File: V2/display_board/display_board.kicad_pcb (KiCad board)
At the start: 2 copper layers, 95 x 103.5 mm, 55 parts, among them J1 Conn_01x12, J2 Conn_01x12, Q1 Si1308EDL, SW1 SW_Push, SW2 SW_Push, SW3 SW_Push, SW4 SW_Push, U1 TPS61165DBV, U2 LTR-303ALS-01, U3 DS18B20Z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

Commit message: main board in good spot
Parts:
- moved J2 134.8 mm to (4.91, 103.1)
- moved J1 41.3 mm to (13.7, 102.8)
- moved C16 6.70 mm to (134.5, 57.5)
- moved U4 6.70 mm to (129.7, 57.1)
- moved H2 6.67 mm to (145.5, 54.5), turned to 180 degrees
- moved H4 6.67 mm to (145.5, 149.0)
- moved C1 3.00 mm to (84.8, 112.7)
- moved C10 3.00 mm to (85.8, 121.2)
- moved C11 3.00 mm to (86.0, 103.8)
- moved C12 3.00 mm to (93.5, 106.0)
- moved C13 3.00 mm to (95.8, 106.8)
- moved C15 3.00 mm to (100.2, 74.7)
- moved C2 3.00 mm to (77.5, 116.2)
- moved C3 3.00 mm to (81.0, 108.2)
- moved C4 3.00 mm to (80.2, 121.2)
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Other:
- board size 95 x 103.5 mm -> 100 x 103.5 mm

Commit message: Display board in good spot
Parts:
- removed J1, J2: Conn_01x12, Connector_PinHeader_2.54mm:PinHeader_1x12_P2.54mm_Vertical_SMD_Pin1Left
- added D7: GREEN, LED_SMD:LED_0805_2012Metric, F.Cu at (65.0, 56.5)
- added D8: RED, LED_SMD:LED_0805_2012Metric, F.Cu at (75.0, 56.5)
- added J5: Conn_02x14_Top_Bottom, Connector_PinHeader_2.54mm:PinHeader_2x14_P2.54mm_Vertical_SMD, B.Cu at (106.0, 100.9)
- added R11: 1.5K, Resistor_SMD:R_0603_1608Metric, F.Cu at (72.5, 56.5)
- added R6: 1.5K, Resistor_SMD:R_0603_1608Metric, F.Cu at (62.5, 56.5)
- added REF**: KiCad-Logo2_12mm_SilkScreen, Symbol:KiCad-Logo2_12mm_SilkScreen, B.Cu at (69.0, 89.0)
- added REF**: OSHW-Logo2_14.6x12mm_SilkScreen, Symbol:OSHW-Logo2_14.6x12mm_SilkScreen, B.Cu at (63.0, 74.0)
- H1, H2, H3, H4: footprint MountingHole:MountingHole_3.2mm_M3_ISO7380_Pad_TopBottom -> MountingHole:MountingHole_3.2mm_M3_ISO7380
- R5: moved to F.Cu
- moved R5 26.9 mm to (80.0, 145.2), turned to 0 degrees
- moved U3 24.0 mm to (76.5, 76.2)
- moved C15 23.9 mm to (76.5, 72.0)
- moved R1 19.1 mm to (68.0, 125.1), turned to 180 degrees
- moved R10 19.0 mm to (77.5, 101.2), turned to -90 degrees
- moved C1 16.3 mm to (68.8, 116.0)
- moved C9 16.2 mm to (86.4, 120.2)
- moved R9 14.8 mm to (74.5, 101.2), turned to -90 degrees
- moved L1 13.1 mm to (68.8, 120.3), turned to -90 degrees
- moved C7 12.4 mm to (83.9, 116.9)
- moved R3 12.0 mm to (87.0, 106.5), turned to 180 degrees
- moved R8 10.5 mm to (71.5, 101.2), turned to -90 degrees
- moved Q1 10.5 mm to (72.6, 120.5), turned to -90 degrees
- moved C8 9.70 mm to (83.9, 120.2)
- moved C3 9.13 mm to (79.2, 117.1), turned to 0 degrees
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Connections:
- net /SCL renamed /I2C_SCL
- net /SDA renamed /I2C_SDA
- C14 pad 1: Net-(U2-VDD) -> +3V3
- C3 pad 1: Net-(D3-K) -> /PREVGH
- D3 pad 1: Net-(D3-K) -> /PREVGH
- U2 pad 1: Net-(U2-VDD) -> +3V3
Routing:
- net +3V3: track 0.00 -> 465.6 mm, vias 0 -> 15
- net /BTN4: track 0.00 -> 210.2 mm, vias 0 -> 3
- net /BTN3: track 0.00 -> 181.6 mm, vias 0 -> 3
- net /BTN2: track 0.00 -> 152.9 mm, vias 0 -> 3
- net /I2C_SCL: track 0.00 -> 150.3 mm, vias 0 -> 2
- net /I2C_SDA: track 0.00 -> 149.6 mm, vias 0 -> 3
- net /BTN1: track 0.00 -> 124.2 mm, vias 0 -> 3
- net /PGOOD: track 0.00 -> 121.4 mm, vias 0 -> 1
- net /CHG: track 0.00 -> 120.8 mm, vias 0 -> 1
- net VPP: track 0.00 -> 116.6 mm, vias 0 -> 4
- net /LED_G: track 0.00 -> 82.1 mm, vias 0 -> 1
- net /DISP_BUSY: track 0.00 -> 70.8 mm, vias 0 -> 2
- net /PRESENCE_TX: track 0.00 -> 70.3 mm, vias 0 -> 1
- net /ALS_INT: track 0.00 -> 68.4 mm, vias 0 -> 1
- net /DISP_RES: track 0.00 -> 67.7 mm, vias 0 -> 2
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- added copper zone on B.Cu, net +3V3
- added copper zone on B.Cu, net GND
- added copper zone on F.Cu, net GND
- added copper zone on B.Cu, net Net-(D1-K)
- added copper zone on B.Cu, net Net-(D3-A)
- added copper zone on B.Cu, net Net-(D4-A)
- added copper zone on B.Cu, net Net-(D4-K)
- added copper zone on B.Cu, net Net-(JP2-C)
- added copper zone on B.Cu, net Net-(U1-FB)
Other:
- outline, holes or cut-outs redrawn
- board text added: "GOOD DISPLAY GDEY042T81-FT02"
- board text added: "HSTAT V2 Display Board 2026"
- board text added: "JLCJLCJLCJLC"
- board text added: "McKay Humpherys Brian Humpherys"

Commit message: Some more tweaks
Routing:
- net +3V3: track 465.6 -> 471.7 mm
- net GND: track 22.4 -> 27.4 mm

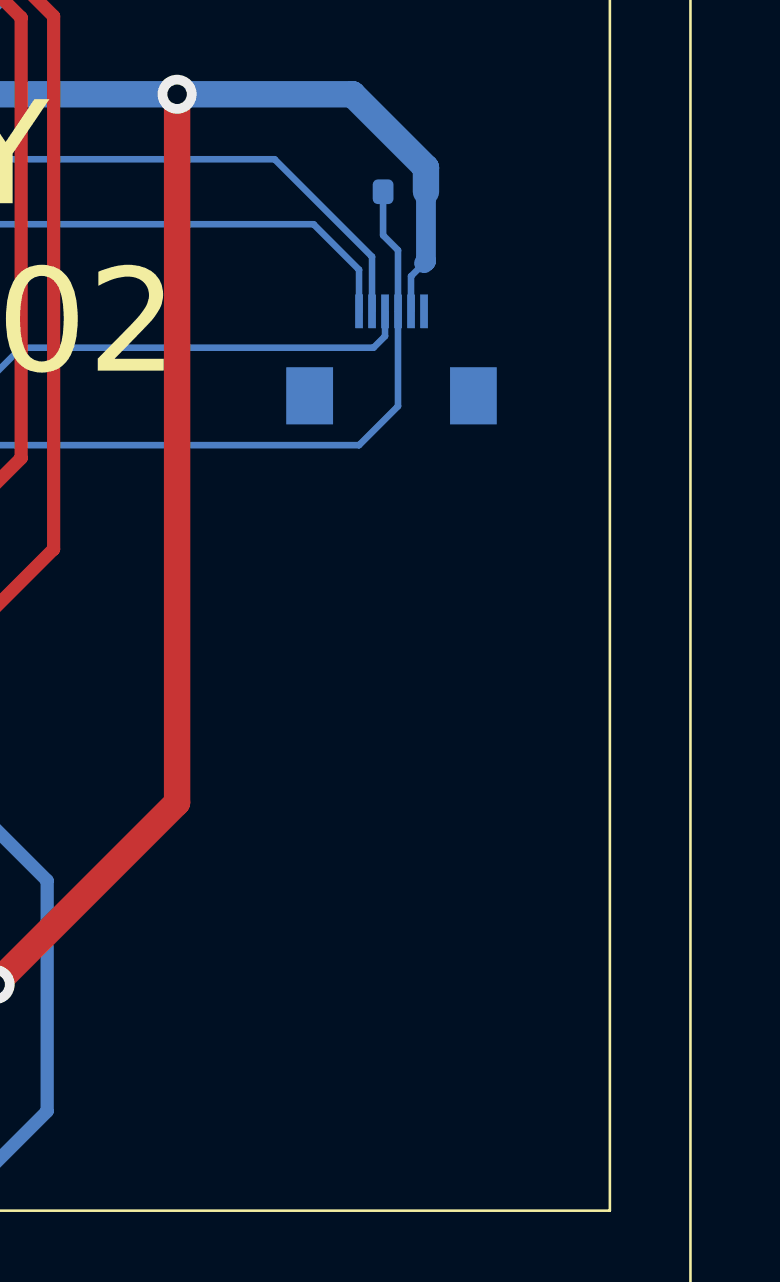
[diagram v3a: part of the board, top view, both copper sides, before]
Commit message: Flip touch screen connector
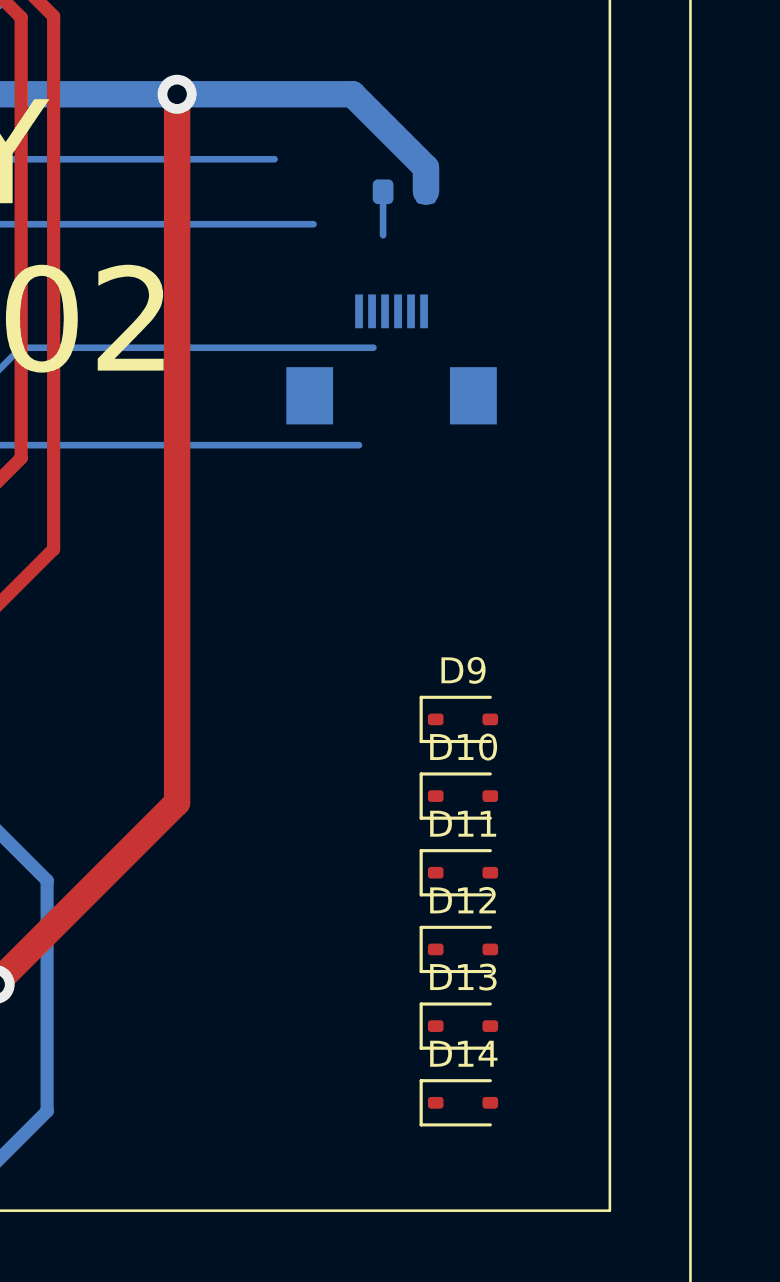
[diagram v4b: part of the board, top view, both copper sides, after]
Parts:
- added D10: D_TVS, Diode_SMD:D_SOD-323, F.Cu at (136.8, 114.0)
- added D11: D_TVS, Diode_SMD:D_SOD-323, F.Cu at (136.8, 117.0)
- added D12: D_TVS, Diode_SMD:D_SOD-323, F.Cu at (136.8, 119.9)
- added D13: D_TVS, Diode_SMD:D_SOD-323, F.Cu at (136.8, 122.8)
- added D14: D_TVS, Diode_SMD:D_SOD-323, F.Cu at (136.8, 125.8)
- added D9: D_TVS, Diode_SMD:D_SOD-323, F.Cu at (136.8, 111.0)
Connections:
- net Net-(D4-K) renamed /LED+
- net Net-(U1-FB) renamed /LED-
- TS1 pad 1: GND -> /I2C_SCL
- TS1 pad 2: +3V3 -> /I2C_SDA
- TS1 pad 3: /TS_RST -> /TS_INT
- TS1 pad 4: /TS_INT -> /TS_RST
- TS1 pad 5: /I2C_SDA -> +3V3
- TS1 pad 6: /I2C_SCL -> GND
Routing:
- net /TS_RST: track 41.9 -> 33.0 mm
- net /I2C_SDA: track 149.6 -> 142.2 mm
- net +3V3: track 471.7 -> 466.8 mm
- net /I2C_SCL: track 150.3 -> 146.2 mm
- net /TS_INT: track 33.9 -> 32.3 mm

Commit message: Fixes
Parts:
- moved D12 67.8 mm to (75.2, 148.4), turned to 90 degrees
- moved D14 61.9 mm to (80.0, 150.6)
- moved D11 52.2 mm to (95.0, 148.3), turned to 90 degrees
- moved D10 40.3 mm to (115.1, 148.0), turned to 90 degrees
- moved D9 37.2 mm to (135.0, 148.2), turned to 90 degrees
- moved D13 33.2 mm to (119.9, 151.5)
- moved R4 1.23 mm to (133.3, 90.7), turned to 0 degrees
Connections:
- J5 pad 23: GND -> /PRESENCE_OUT
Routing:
- net /PRESENCE_OUT: track 6.92 -> 102.7 mm, vias 0 -> 1
- net /I2C_SDA: track 142.2 -> 151.9 mm, vias 3 -> 5
- net /TS_RST: track 33.0 -> 41.7 mm, vias 0 -> 2
- net /I2C_SCL: track 146.2 -> 153.3 mm, vias 2 -> 4
- net /ADDR_LED: track 53.7 -> 56.4 mm
- net +3V3: track 466.8 -> 469.5 mm
- net /BTN1: track 124.2 -> 126.8 mm
- net /LED_G: track 82.1 -> 84.5 mm
- net /BTN2: track 152.9 -> 155.3 mm
- net /BTN3: track 181.6 -> 183.9 mm
- net /BTN4: track 210.2 -> 212.6 mm
- net /TS_INT: track 32.3 -> 34.3 mm
- net GND: vias 0 -> 3

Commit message: Final updates
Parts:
- renumbered J5 to J1
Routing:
- net GND: vias 3 -> 8
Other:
- board text added: "CHG"
- board text added: "PGOOD"
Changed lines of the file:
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@@
 		(descr "surface-mounted straight pin header, 2x14, 2.54mm pitch, double rows")
 		(tags "Surface mounted pin header SMD 2x14 2.54mm double row")
-		(property "Reference" "J5"
+		(property "Reference" "J1"
 			(at 0 18.89 0)
 			(layer "B.SilkS")
@@
 		(layer "Edge.Cuts")
 	)
+	(gr_text "CHG"
+		(at 75 54.25 0)
+		(layer "F.SilkS")
+		(effects
+			(font
+				(size 1.5 1.5)
+				(thickness 0.1875)
+			)
+			(justify bottom)
+		)
+	)
 	(gr_text "JLCJLCJLCJLC"
 		(at 100 71.25 0)
@@
 		)
 	)
+	(gr_text "PGOOD"
+		(at 65 54.25 0)
+		(layer "F.SilkS")
+		(effects
+			(font
+				(size 1.5 1.5)
+				(thickness 0.1875)
+			)
+			(justify bottom)
+		)
+	)
 	(gr_text "HSTAT V2\nDisplay Board\n2026"
 		(at 130 66.5 0)
@@
 	)
 	(via
+		(at 86.75 86)
+		(size 0.762)
+		(drill 0.381)
+		(layers "F.Cu" "B.Cu")
+		(free yes)
+		(net 2)
+	)
+	(via
+		(at 94.75 88.25)
+		(size 0.762)
+		(drill 0.381)
+		(layers "F.Cu" "B.Cu")
+		(free yes)
+		(net 2)
+	)
+	(via
+		(at 91.75 85.75)
+		(size 0.762)
+		(drill 0.381)
+		(layers "F.Cu" "B.Cu")
+		(free yes)
+		(net 2)
+	)
+	(via
 		(at 74.1 127.1)
 		(size 0.762)
@@
 	)
 	(via
+		(at 129.25 68.75)
+		(size 0.762)
+		(drill 0.381)
+		(layers "F.Cu" "B.Cu")
+		(free yes)
+		(net 2)
+	)
+	(via
 		(at 73 128.1)
 		(size 0.762)
@@
 	)
 	(via
+		(at 88.75 88.25)
+		(size 0.762)
+		(drill 0.381)
+		(layers "F.Cu" "B.Cu")
+		(free yes)
+		(net 2)
+	)
+	(via
 		(at 73 127.1)
 		(size 0.762)
@@
 			(thermal_gap 0.35)
 			(thermal_bridge_width 0.5)
+			(island_removal_mode 2)
+			(island_area_min 10)
 		)
 		(polygon
